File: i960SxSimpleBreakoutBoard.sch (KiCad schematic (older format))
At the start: 31 parts, among them J1 Control Lines, J2 Address Lines, J3 Data Lines, U1 80960Sx, U2 74HC573, U3 74HC573, U4 74HC245, U5 74HC245

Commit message: Widen the board to make routing easier
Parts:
- J1: footprint Connector_PinHeader_2.54mm:PinHeader_1x12_P2.54mm_Vertical -> Connector_PinHeader_2.54mm:PinHeader_2x12_P2.54mm_Vertical
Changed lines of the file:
@@
 F 0 "J1" H 13750 2417 50  0000 C CNN
 F 1 "Control Lines" H 13750 2326 50  0000 C CNN
-F 2 "Connector_PinHeader_2.54mm:PinHeader_1x12_P2.54mm_Vertical" H 13700 1700 50  0001 C CNN
+F 2 "Connector_PinHeader_2.54mm:PinHeader_2x12_P2.54mm_Vertical" H 13700 1700 50  0001 C CNN
 F 3 "~" H 13700 1700 50  0001 C CNN
 	1    13700 1700

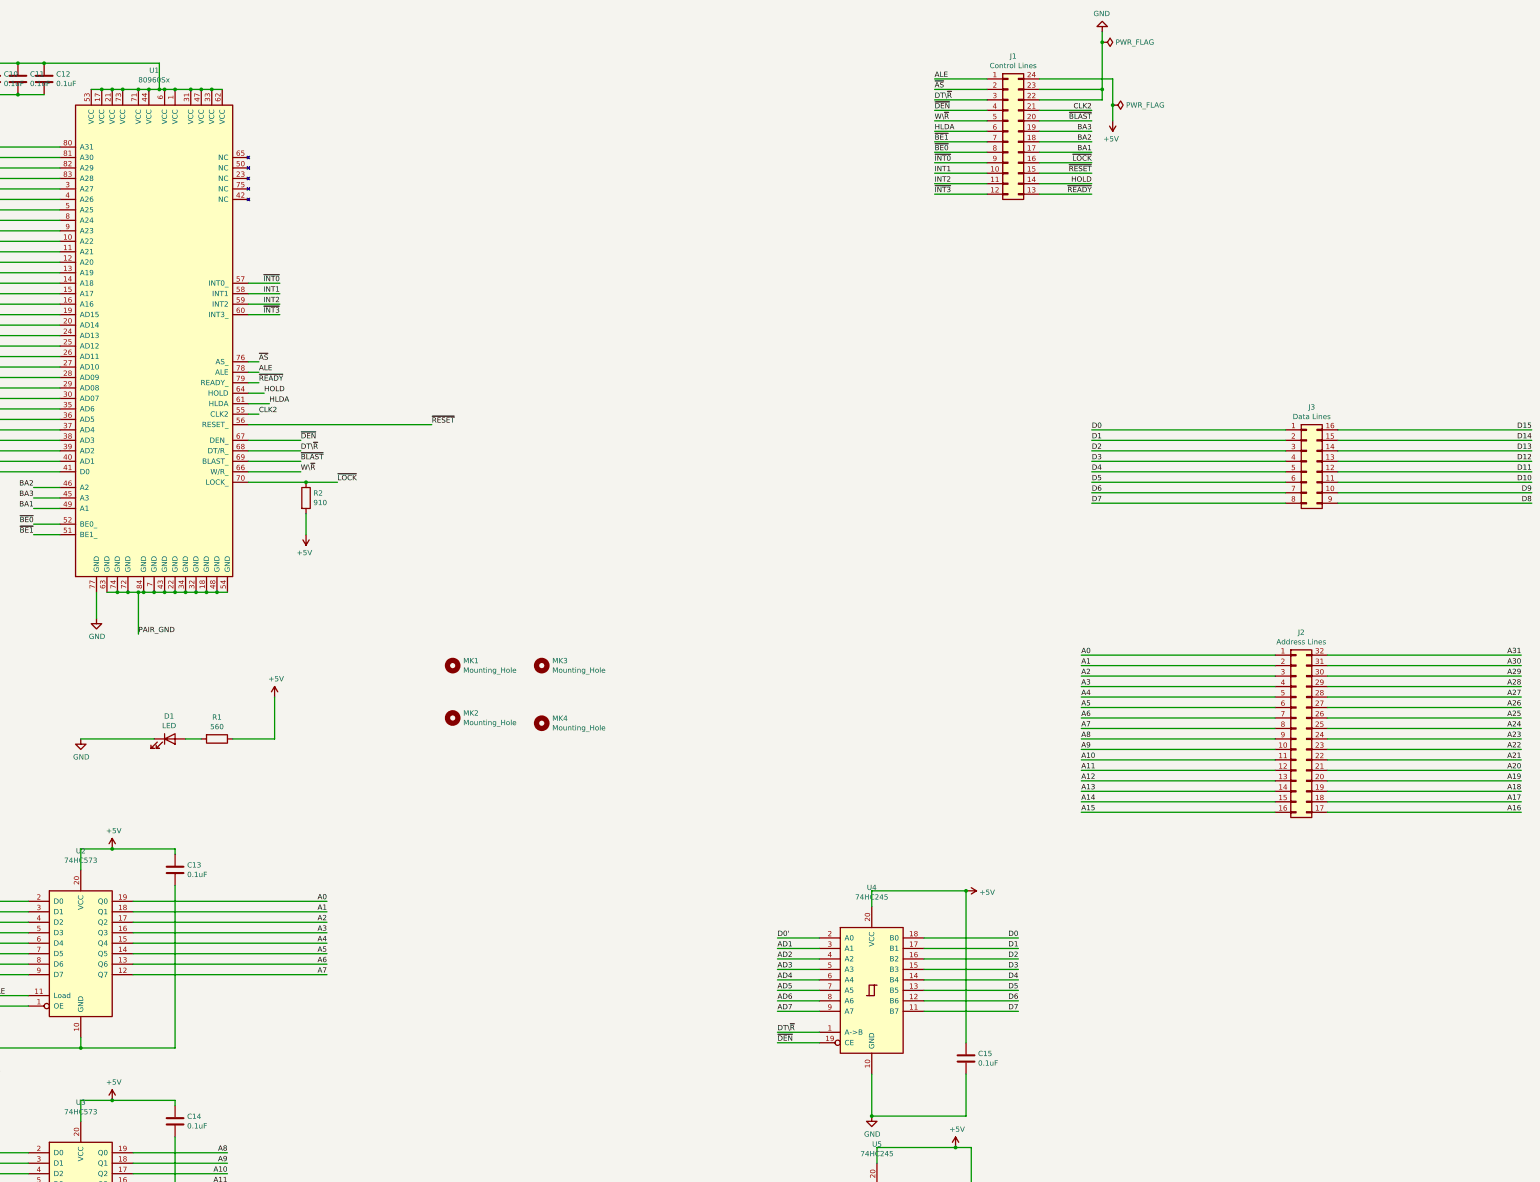
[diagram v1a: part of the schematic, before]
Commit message: Use single row headers in all cases now
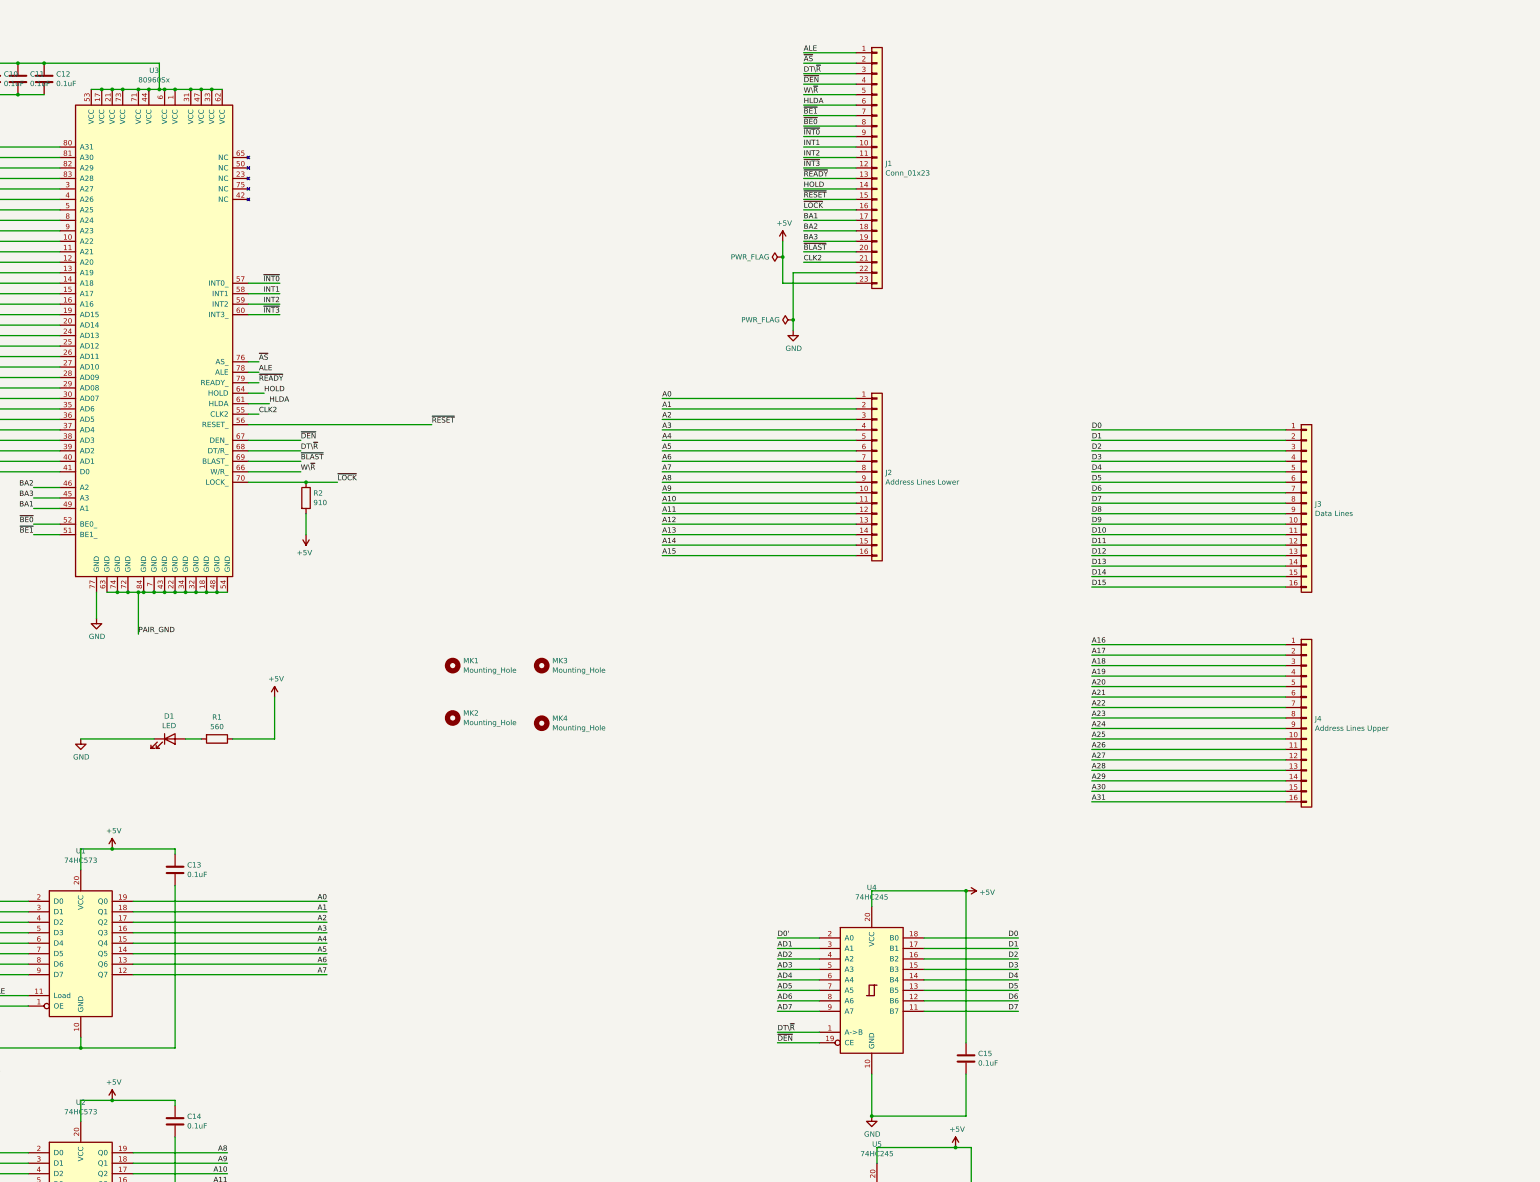
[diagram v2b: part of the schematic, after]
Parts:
- removed J1: Control Lines, Connector_PinHeader_2.54mm:PinHeader_2x12_P2.54mm_Vertical, symbol Connector_Generic:Conn_02x12_Counter_Clockwise
- removed J2: Address Lines, Connector_PinHeader_2.54mm:PinHeader_2x16_P2.54mm_Vertical, symbol Connector_Generic:Conn_02x16_Counter_Clockwise
- removed J3: Data Lines, Connector_PinHeader_2.54mm:PinHeader_2x08_P2.54mm_Vertical, symbol Connector_Generic:Conn_02x08_Counter_Clockwise
- added J1: Conn_01x23, Connector_PinHeader_2.54mm:PinHeader_1x23_P2.54mm_Vertical, symbol Connector_Generic:Conn_01x23
- added J2: Address Lines Lower, Connector_PinHeader_2.54mm:PinHeader_1x16_P2.54mm_Vertical, symbol Connector_Generic:Conn_01x16
- added J3: Data Lines, Connector_PinHeader_2.54mm:PinHeader_1x16_P2.54mm_Vertical, symbol Connector_Generic:Conn_01x16
- added J4: Address Lines Upper, Connector_PinHeader_2.54mm:PinHeader_1x16_P2.54mm_Vertical, symbol Connector_Generic:Conn_01x16
- renumbered U2 to U1, U3 to U2, U1 to U3
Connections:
- net +5V: now also J1.23 (Pin_23)
- net A0: now also J2.1 (Pin_1)
- net A1: now also J2.2 (Pin_2)
- net A10: now also J2.11 (Pin_11)
- net A11: now also J2.12 (Pin_12)
- net A12: now also J2.13 (Pin_13)
- net A13: now also J2.14 (Pin_14)
- net A14: now also J2.15 (Pin_15)
- net A15: now also J2.16 (Pin_16)
- net A16: now also J4.1 (Pin_1)
- net A17: now also J4.2 (Pin_2)
- net A18: now also J4.3 (Pin_3)
- net A19: now also J4.4 (Pin_4)
- net A2: now also J2.3 (Pin_3)
- net A20: now also J4.5 (Pin_5)
- net A21: now also J4.6 (Pin_6)
- net A22: now also J4.7 (Pin_7)
- net A23: now also J4.8 (Pin_8)
- net A24: now also J4.9 (Pin_9)
- net A25: now also J4.10 (Pin_10)
- net A26: now also J4.11 (Pin_11)
- net A27: now also J4.12 (Pin_12)
- net A28: now also J4.13 (Pin_13)
- net A29: now also J4.14 (Pin_14)
- net A3: now also J2.4 (Pin_4)
- net A30: now also J4.15 (Pin_15)
- net A31: now also J4.16 (Pin_16)
- net A4: now also J2.5 (Pin_5)
- net A5: now also J2.6 (Pin_6)
- net A6: now also J2.7 (Pin_7)
- net A7: now also J2.8 (Pin_8)
- net A8: now also J2.9 (Pin_9)
- net A9: now also J2.10 (Pin_10)
- net ALE: now also J1.1 (Pin_1)
- net BA1: now also J1.17 (Pin_17)
- net BA2: now also J1.18 (Pin_18)
- net BA3: now also J1.19 (Pin_19)
- net CLK2: now also J1.21 (Pin_21)
- net D0: now also J3.1 (Pin_1)
- net D1: now also J3.2 (Pin_2)
- net D10: now also J3.11 (Pin_11)
- net D11: now also J3.12 (Pin_12)
- net D12: now also J3.13 (Pin_13)
- net D13: now also J3.14 (Pin_14)
- net D14: now also J3.15 (Pin_15)
- net D15: now also J3.16 (Pin_16)
- net D2: now also J3.3 (Pin_3)
- net D3: now also J3.4 (Pin_4)
- net D4: now also J3.5 (Pin_5)
- net D5: now also J3.6 (Pin_6)
- net D6: now also J3.7 (Pin_7)
- net D7: now also J3.8 (Pin_8)
- net D8: now also J3.9 (Pin_9)
- net D9: now also J3.10 (Pin_10)
- net DT\~R: now also J1.3 (Pin_3)
- net GND: now also J1.22 (Pin_22)
- net HLDA: now also J1.6 (Pin_6)
- net HOLD: now also J1.14 (Pin_14)
- net INT1: now also J1.10 (Pin_10)
- net INT2: now also J1.11 (Pin_11)
- net W\~R: now also J1.5 (Pin_5)
- net ~AS: now also J1.2 (Pin_2)
- net ~BE0: now also J1.8 (Pin_8)
- net ~BE1: now also J1.7 (Pin_7)
- net ~BLAST: now also J1.20 (Pin_20)
- net ~DEN: now also J1.4 (Pin_4)
- net ~INT0: now also J1.9 (Pin_9)
- net ~INT3: now also J1.12 (Pin_12)
- net ~LOCK: now also J1.16 (Pin_16)
- net ~READY: now also J1.13 (Pin_13)
- net ~RESET: now also J1.15 (Pin_15)

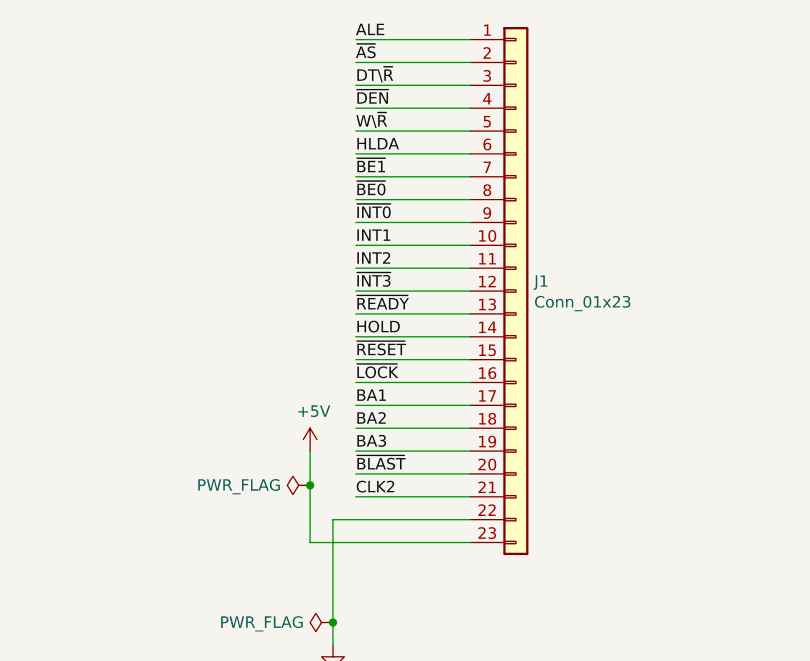
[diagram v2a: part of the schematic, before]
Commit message: Modify pinout of control signals to make routing of traces easier
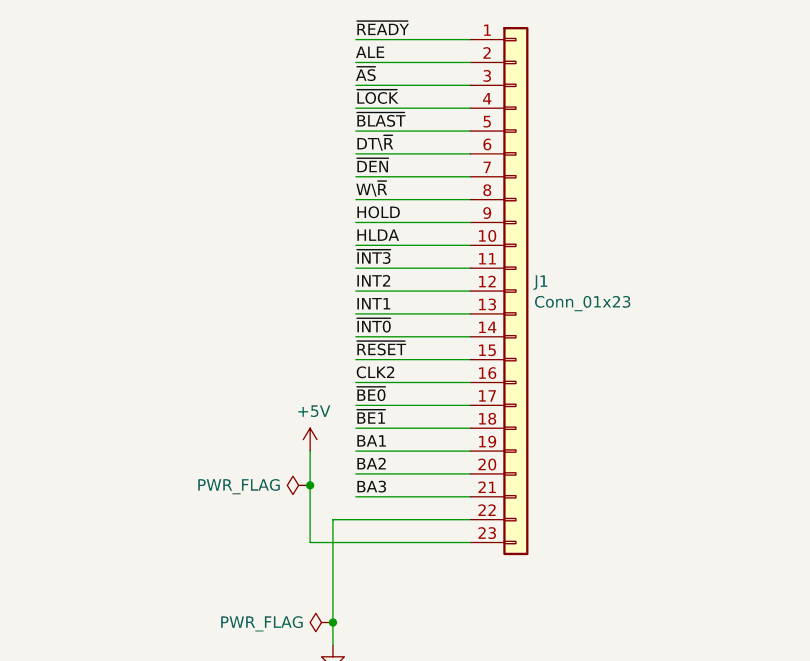
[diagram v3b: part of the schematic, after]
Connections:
- net ALE: now also J1.2 (Pin_2); no longer J1.1 (Pin_1)
- net BA1: now also J1.19 (Pin_19); no longer J1.17 (Pin_17)
- net BA2: now also J1.20 (Pin_20); no longer J1.18 (Pin_18)
- net BA3: now also J1.21 (Pin_21); no longer J1.19 (Pin_19)
- net CLK2: now also J1.16 (Pin_16); no longer J1.21 (Pin_21)
- net DT\~R: now also J1.6 (Pin_6); no longer J1.3 (Pin_3)
- net HLDA: now also J1.10 (Pin_10); no longer J1.6 (Pin_6)
- net HOLD: now also J1.9 (Pin_9); no longer J1.14 (Pin_14)
- net INT1: now also J1.13 (Pin_13); no longer J1.10 (Pin_10)
- net INT2: now also J1.12 (Pin_12); no longer J1.11 (Pin_11)
- net W\~R: now also J1.8 (Pin_8); no longer J1.5 (Pin_5)
- net ~AS: now also J1.3 (Pin_3); no longer J1.2 (Pin_2)
- net ~BE0: now also J1.17 (Pin_17); no longer J1.8 (Pin_8)
- net ~BE1: now also J1.18 (Pin_18); no longer J1.7 (Pin_7)
- net ~BLAST: now also J1.5 (Pin_5); no longer J1.20 (Pin_20)
- net ~DEN: now also J1.7 (Pin_7); no longer J1.4 (Pin_4)
- net ~INT0: now also J1.14 (Pin_14); no longer J1.9 (Pin_9)
- net ~INT3: now also J1.11 (Pin_11); no longer J1.12 (Pin_12)
- net ~LOCK: now also J1.4 (Pin_4); no longer J1.16 (Pin_16)
- net ~READY: now also J1.1 (Pin_1); no longer J1.13 (Pin_13)
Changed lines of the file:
@@
 Text Label 11750 2350 0    50   ~ 0
 ~RESET
-Text Label 11750 2950 0    50   ~ 0
+Text Label 11750 2450 0    50   ~ 0
 CLK2
 Wire Wire Line
 	11750 2950 12250 2950
-Text Label 11750 2250 0    50   ~ 0
+Text Label 11750 1750 0    50   ~ 0
 HOLD
-Text Label 11750 2150 0    50   ~ 0
+Text Label 11750 950  0    50   ~ 0
 ~READY
 Wire Wire Line
@@
 Wire Wire Line
 	11750 2150 12250 2150
-Text Label 11750 2450 0    50   ~ 0
+Text Label 11750 1250 0    50   ~ 0
 ~LOCK
 Wire Wire Line
@@
 Wire Wire Line
 	11750 2750 12250 2750
-Text Label 11750 2850 0    50   ~ 0
+Text Label 11750 1350 0    50   ~ 0
 ~BLAST
 Wire Wire Line
 	12250 2850 11750 2850
-Text Label 11750 2550 0    50   ~ 0
+Text Label 11750 2750 0    50   ~ 0
 BA1
-Text Label 11750 2750 0    50   ~ 0
+Text Label 11750 2950 0    50   ~ 0
 BA3
-Text Label 11750 2650 0    50   ~ 0
+Text Label 11750 2850 0    50   ~ 0
 BA2
 Wire Wire Line
@@
 Wire Wire Line
 	11750 1850 12250 1850
+Text Label 11750 2050 0    50   ~ 0
+INT2
+Text Label 11750 2150 0    50   ~ 0
+INT1
 Text Label 11750 1950 0    50   ~ 0
-INT2
-Text Label 11750 1850 0    50   ~ 0
-INT1
-Text Label 11750 2050 0    50   ~ 0
 ~INT3
 Wire Wire Line
 	11750 950  12250 950
-Text Label 11750 950  0    50   ~ 0
+Text Label 11750 1050 0    50   ~ 0
 ALE
 Wire Wire Line
@@
 Wire Wire Line
 	11750 1650 12250 1650
-Text Label 11750 1550 0    50   ~ 0
+Text Label 11750 2650 0    50   ~ 0
 ~BE1
-Text Label 11750 1650 0    50   ~ 0
+Text Label 11750 2550 0    50   ~ 0
 ~BE0
 Wire Wire Line
 	11750 1750 12250 1750
-Text Label 11750 1750 0    50   ~ 0
+Text Label 11750 2250 0    50   ~ 0
 ~INT0
-Text Label 11750 1050 0    50   ~ 0
+Text Label 11750 1150 0    50   ~ 0
 ~AS
 Wire Wire Line
 	11750 1050 12250 1050
-Text Label 11750 1250 0    50   ~ 0
+Text Label 11750 1550 0    50   ~ 0
 ~DEN
-Text Label 11750 1150 0    50   ~ 0
+Text Label 11750 1450 0    50   ~ 0
 DT\~R
-Text Label 11750 1350 0    50   ~ 0
+Text Label 11750 1650 0    50   ~ 0
 W\~R
 Wire Wire Line
 	11750 1450 12250 1450
-Text Label 11750 1450 0    50   ~ 0
+Text Label 11750 1850 0    50   ~ 0
 HLDA
 Wire Wire Line

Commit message: Get rid of the mounting holes and put multiplexed lines on a single edge
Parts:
- removed MK1, MK2, MK3, MK4: Mounting_Hole, MountingHole:MountingHole_3.2mm_M3, symbol mechanical:Mounting_Hole
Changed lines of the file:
@@
 Text Label 8200 4500 0    50   ~ 0
 ~RESET
-$Comp
-L mechanical:Mounting_Hole MK1
-U 1 1 60038A23
-P 8400 6800
-F 0 "MK1" H 8500 6846 50  0000 L CNN
-F 1 "Mounting_Hole" H 8500 6755 50  0000 L CNN
-F 2 "MountingHole:MountingHole_3.2mm_M3" H 8400 6800 50  0001 C CNN
-F 3 "" H 8400 6800 50  0001 C CNN
-	1    8400 6800
-	1    0    0    -1
-$EndComp
-$Comp
-L mechanical:Mounting_Hole MK3
-U 1 1 60038C4E
-P 9250 6800
-F 0 "MK3" H 9350 6846 50  0000 L CNN
-F 1 "Mounting_Hole" H 9350 6755 50  0000 L CNN
-F 2 "MountingHole:MountingHole_3.2mm_M3" H 9250 6800 50  0001 C CNN
-F 3 "" H 9250 6800 50  0001 C CNN
-	1    9250 6800
-	1    0    0    -1
-$EndComp
-$Comp
-L mechanical:Mounting_Hole MK2
-U 1 1 60038F7C
-P 8400 7300
-F 0 "MK2" H 8500 7346 50  0000 L CNN
-F 1 "Mounting_Hole" H 8500 7255 50  0000 L CNN
-F 2 "MountingHole:MountingHole_3.2mm_M3" H 8400 7300 50  0001 C CNN
-F 3 "" H 8400 7300 50  0001 C CNN
-	1    8400 7300
-	1    0    0    -1
-$EndComp
-$Comp
-L mechanical:Mounting_Hole MK4
-U 1 1 600390A6
-P 9250 7350
-F 0 "MK4" H 9350 7396 50  0000 L CNN
-F 1 "Mounting_Hole" H 9350 7305 50  0000 L CNN
-F 2 "MountingHole:MountingHole_3.2mm_M3" H 9250 7350 50  0001 C CNN
-F 3 "" H 9250 7350 50  0001 C CNN
-	1    9250 7350
-	1    0    0    -1
-$EndComp
 Wire Wire Line
 	5550 7500 4850 7500
